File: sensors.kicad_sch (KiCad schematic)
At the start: 7 parts

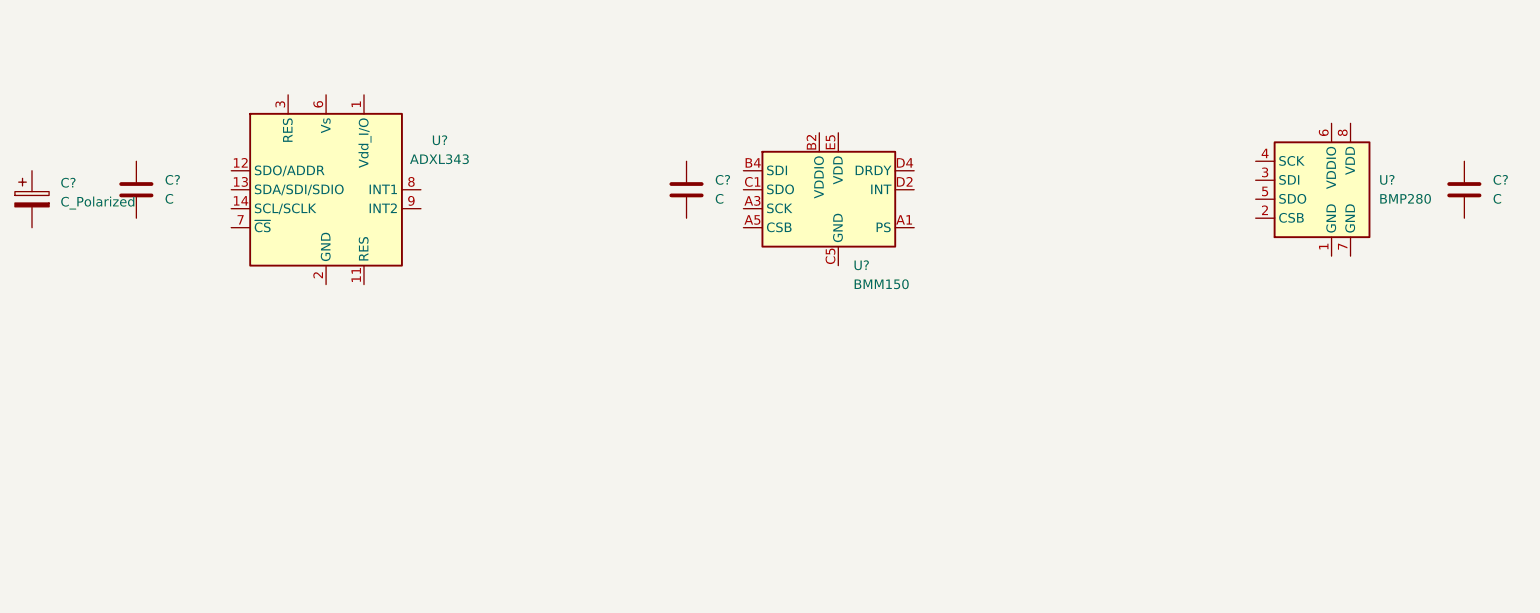
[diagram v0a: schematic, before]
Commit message: Refactor the mainboard
- Use smaller STM
- Use MPU-9250 as a motion sensor
- Connect some peripherals to the MCU
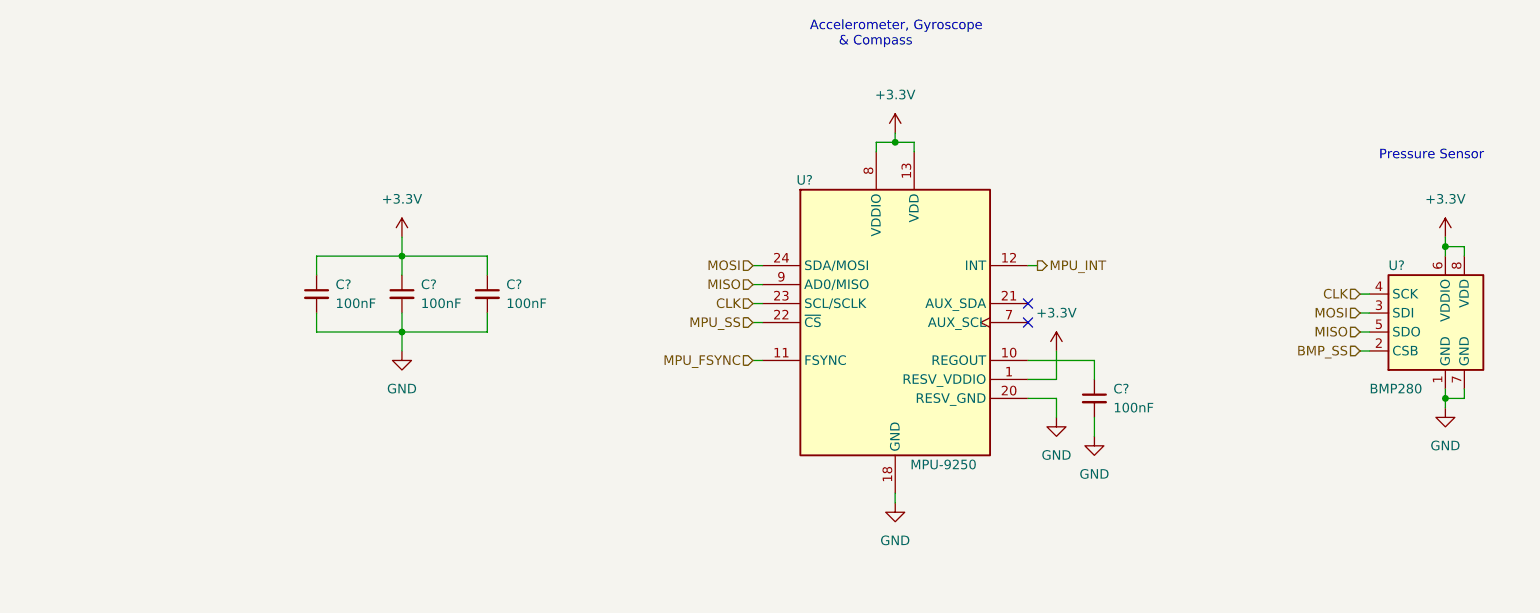
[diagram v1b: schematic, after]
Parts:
- removed C?: C_Polarized, symbol Device:C_Polarized
- removed C? (x3): C, symbol Device:C
- removed U?: BMM150, Package_CSP:WLCSP-12_1.56x1.56mm_P0.4mm, symbol Sensor_Magnetic:BMM150
- removed U?: ADXL343, Package_LGA:LGA-14_3x5mm_P0.8mm_LayoutBorder1x6y, symbol Sensor_Motion:ADXL343
- added C? (x4): 100nF, symbol Device:C_Small
- added U?: MPU-9250, Sensor_Motion:InvenSense_QFN-24_3x3mm_P0.4mm, symbol Sensor_Motion:MPU-9250
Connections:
- net GND: now reaches U?.1 (GND)
- net GND: now also U?.7 (GND), C?.2, C?.2, C?.2, C?.2, U?.18 (GND), U?.20 (RESV_GND)
- net BMP_SS: now reaches U?.2 (CSB)
- net MOSI: now reaches U?.3 (SDI)
- net MOSI: now also U?.24 (SDA/MOSI)
- net CLK: now reaches U?.4 (SCK)
- net CLK: now also U?.23 (SCL/SCLK)
- net MISO: now reaches U?.5 (SDO)
- net MISO: now also U?.9 (AD0/MISO)
- net +3.3V: now reaches U?.6 (VDDIO)
- net +3.3V: now also U?.8 (VDD), C?.1, C?.1, C?.1, U?.1 (RESV_VDDIO), U?.13 (VDD), U?.8 (VDDIO)
- new net: C?.1, U?.10 (REGOUT)
- new net MPU_FSYNC: U?.11 (FSYNC)
- new net MPU_INT: U?.12 (INT)
- new net MPU_SS: U?.22 (~{CS})
- no-connect marks 0 -> 2
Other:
- note added: "Accelerometer, Gyroscope & Compass"
- note added: "Pressure Sensor"
- moved on the sheet: U?

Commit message: Connect sensors to the MCU
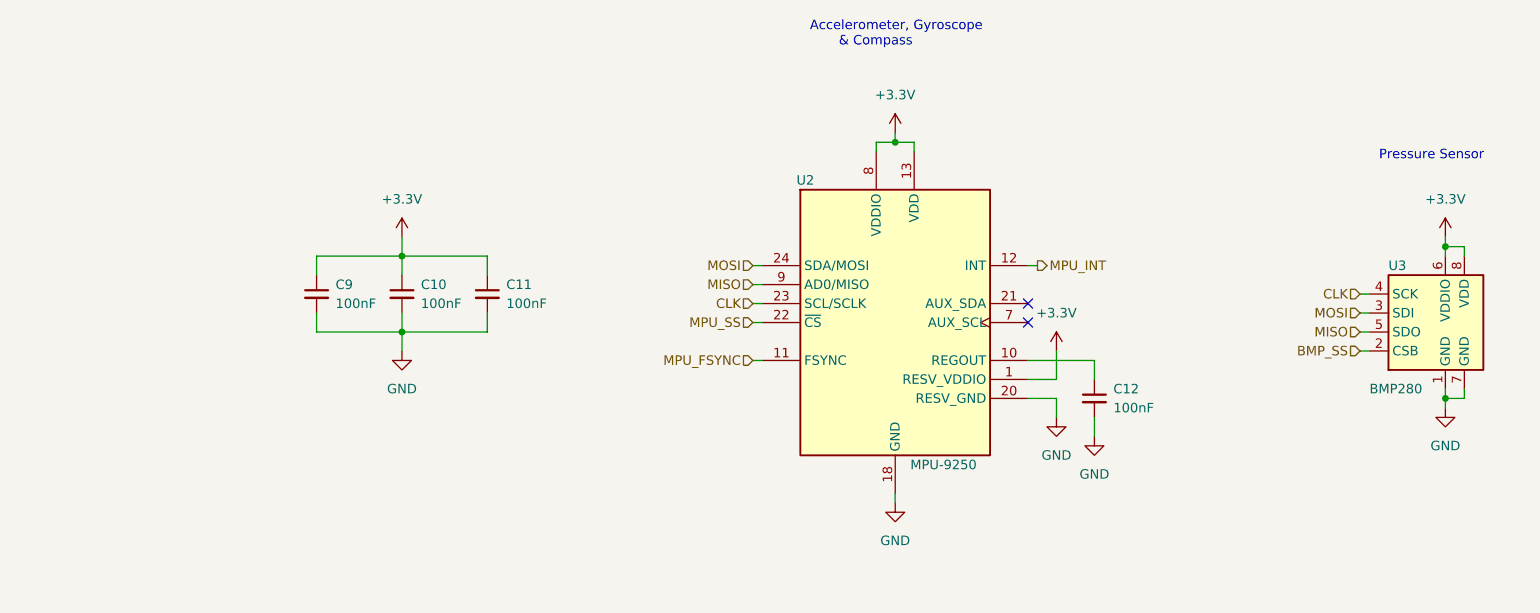
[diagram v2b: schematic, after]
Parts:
- gave numbers to parts that had none: 6
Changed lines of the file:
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@@
   (paper "A4")
   (title_block
-    (date "2022-11-22")
+    (date "2022-12-16")
     (rev "0.1.0")
   )
@@
   (symbol (lib_id "power:+3.3V") (at 222.25 81.28 0) (unit 1)
     (in_bom yes) (on_board yes) (fields_autoplaced)
-    (property "Reference" "#PWR?" (id 0) (at 222.25 85.09 0)
+    (property "Reference" "#PWR0120" (id 0) (at 222.25 85.09 0)
       (effects (font (size 1.27 1.27)) hide)
     )
@@
   (symbol (lib_id "Device:C_Small") (at 93.98 88.9 0) (unit 1)
     (in_bom yes) (on_board yes) (fields_autoplaced)
-    (property "Reference" "C?" (id 0) (at 96.52 87.6362 0)
+    (property "Reference" "C11" (id 0) (at 96.52 87.6362 0)
       (effects (font (size 1.27 1.27)) (justify left))
     )
@@
   (symbol (lib_id "power:+3.3V") (at 82.55 81.28 0) (unit 1)
     (in_bom yes) (on_board yes) (fields_autoplaced)
-    (property "Reference" "#PWR?" (id 0) (at 82.55 85.09 0)
+    (property "Reference" "#PWR0117" (id 0) (at 82.55 85.09 0)
       (effects (font (size 1.27 1.27)) hide)
     )
@@
   (symbol (lib_id "power:GND") (at 170.18 105.41 0) (unit 1)
     (in_bom yes) (on_board yes)
-    (property "Reference" "#PWR?" (id 0) (at 170.18 111.76 0)
+    (property "Reference" "#PWR0122" (id 0) (at 170.18 111.76 0)
       (effects (font (size 1.27 1.27)) hide)
     )
@@
   (symbol (lib_id "power:GND") (at 175.26 107.95 0) (unit 1)
     (in_bom yes) (on_board yes) (fields_autoplaced)
-    (property "Reference" "#PWR?" (id 0) (at 175.26 114.3 0)
+    (property "Reference" "#PWR0123" (id 0) (at 175.26 114.3 0)
       (effects (font (size 1.27 1.27)) hide)
     )
@@
   (symbol (lib_id "power:+3.3V") (at 170.18 96.52 0) (unit 1)
     (in_bom yes) (on_board yes) (fields_autoplaced)
-    (property "Reference" "#PWR?" (id 0) (at 170.18 100.33 0)
+    (property "Reference" "#PWR0121" (id 0) (at 170.18 100.33 0)
       (effects (font (size 1.27 1.27)) hide)
     )
@@
   (symbol (lib_id "power:GND") (at 148.59 116.84 0) (unit 1)
     (in_bom yes) (on_board yes) (fields_autoplaced)
-    (property "Reference" "#PWR?" (id 0) (at 148.59 123.19 0)
+    (property "Reference" "#PWR0116" (id 0) (at 148.59 123.19 0)
       (effects (font (size 1.27 1.27)) hide)
     )
@@
   (symbol (lib_id "Sensor_Pressure:BMP280") (at 222.25 93.98 0) (unit 1)
     (in_bom yes) (on_board yes)
-    (property "Reference" "U?" (id 0) (at 214.63 85.0899 0)
+    (property "Reference" "U3" (id 0) (at 214.63 85.0899 0)
       (effects (font (size 1.27 1.27)) (justify left))
     )
@@
   (symbol (lib_id "power:GND") (at 222.25 104.14 0) (unit 1)
     (in_bom yes) (on_board yes) (fields_autoplaced)
-    (property "Reference" "#PWR?" (id 0) (at 222.25 110.49 0)
+    (property "Reference" "#PWR0119" (id 0) (at 222.25 110.49 0)
       (effects (font (size 1.27 1.27)) hide)
     )
@@
   (symbol (lib_id "Device:C_Small") (at 175.26 102.87 0) (unit 1)
     (in_bom yes) (on_board yes) (fields_autoplaced)
-    (property "Reference" "C?" (id 0) (at 177.8 101.6062 0)
+    (property "Reference" "C12" (id 0) (at 177.8 101.6062 0)
       (effects (font (size 1.27 1.27)) (justify left))
     )
@@
   (symbol (lib_id "Device:C_Small") (at 82.55 88.9 0) (unit 1)
     (in_bom yes) (on_board yes) (fields_autoplaced)
-    (property "Reference" "C?" (id 0) (at 85.09 87.6362 0)
+    (property "Reference" "C10" (id 0) (at 85.09 87.6362 0)
       (effects (font (size 1.27 1.27)) (justify left))
     )
@@
   (symbol (lib_id "Device:C_Small") (at 71.12 88.9 0) (unit 1)
     (in_bom yes) (on_board yes) (fields_autoplaced)
-    (property "Reference" "C?" (id 0) (at 73.66 87.6362 0)
+    (property "Reference" "C9" (id 0) (at 73.66 87.6362 0)
       (effects (font (size 1.27 1.27)) (justify left))
     )
@@
   (symbol (lib_id "Sensor_Motion:MPU-9250") (at 148.59 92.71 0) (unit 1)
     (in_bom yes) (on_board yes)
-    (property "Reference" "U?" (id 0) (at 135.3694 73.66 0)
+    (property "Reference" "U2" (id 0) (at 135.3694 73.66 0)
       (effects (font (size 1.27 1.27)) (justify left))
     )
@@
   (symbol (lib_id "power:+3.3V") (at 148.59 67.31 0) (unit 1)
     (in_bom yes) (on_board yes) (fields_autoplaced)
-    (property "Reference" "#PWR?" (id 0) (at 148.59 71.12 0)
+    (property "Reference" "#PWR0118" (id 0) (at 148.59 71.12 0)
       (effects (font (size 1.27 1.27)) hide)
     )
@@
   (symbol (lib_id "power:GND") (at 82.55 96.52 0) (unit 1)
     (in_bom yes) (on_board yes) (fields_autoplaced)
-    (property "Reference" "#PWR?" (id 0) (at 82.55 102.87 0)
-      (effects (font (size 1.27 1.27)) hide)
-    )
+    (property "Reference" "#PWR0115" (id 0) (at 82.55 102.87 0)
+      (effects (font (size 1.27 1.27)) hide)
+    )

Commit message: Improve the power section:
- add ADC circuit to measure battery level
- add 5V LDO regulator
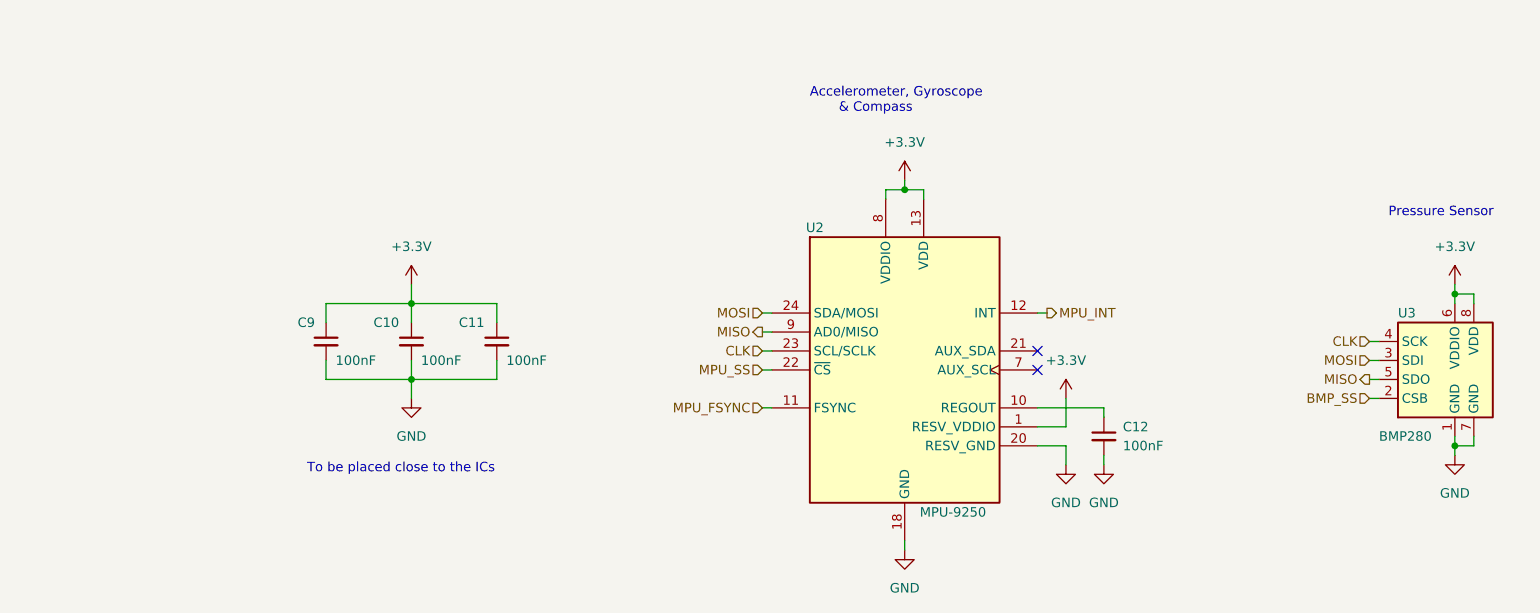
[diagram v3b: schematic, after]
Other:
- note added: "To be placed close to the ICs"
- title: (none) -> Sensors
- moved on the sheet: C10, C11, C12, C9, U2, U3

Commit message: Assign footprints to symbols
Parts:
- C17: renamed from C9; footprint (none) -> Capacitor_SMD:C_0603_1608Metric
- C18: renamed from C10; footprint (none) -> Capacitor_SMD:C_0603_1608Metric
- C19: renamed from C11; footprint (none) -> Capacitor_SMD:C_0603_1608Metric
- C20: renamed from C12; footprint (none) -> Capacitor_SMD:C_0603_1608Metric
- renumbered U2 to U7, U3 to U8
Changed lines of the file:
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@@
     (title "Sensors")
     (date "2022-12-17")
-    (rev "0.1.0")
+    (rev "${REVISION}")
   )
   (junction (at 223.52 88.9) (diameter 0) (color 0 0 0 0)
@@
   (symbol (lib_id "power:+3.3V") (at 223.52 87.63 0) (unit 1)
     (in_bom yes) (on_board yes) (fields_autoplaced)
-    (property "Reference" "#PWR017" (id 0) (at 223.52 91.44 0)
+    (property "Reference" "#PWR044" (id 0) (at 223.52 91.44 0)
       (effects (font (size 1.27 1.27)) hide)
     )
@@
   (symbol (lib_id "Device:C_Small") (at 95.25 95.25 0) (unit 1)
     (in_bom yes) (on_board yes)
-    (property "Reference" "C11" (id 0) (at 90.17 92.7162 0)
+    (property "Reference" "C19" (id 0) (at 90.17 92.7162 0)
       (effects (font (size 1.27 1.27)) (justify left))
     )
@@
       (effects (font (size 1.27 1.27)) (justify left))
     )
-    (property "Footprint" "" (id 2) (at 95.25 95.25 0)
+    (property "Footprint" "Capacitor_SMD:C_0603_1608Metric" (id 2) (at 95.25 95.25 0)
       (effects (font (size 1.27 1.27)) hide)
     )
@@
   (symbol (lib_id "power:+3.3V") (at 83.82 87.63 0) (unit 1)
     (in_bom yes) (on_board yes) (fields_autoplaced)
-    (property "Reference" "#PWR016" (id 0) (at 83.82 91.44 0)
+    (property "Reference" "#PWR043" (id 0) (at 83.82 91.44 0)
       (effects (font (size 1.27 1.27)) hide)
     )
@@
   (symbol (lib_id "power:GND") (at 171.45 111.76 0) (unit 1)
     (in_bom yes) (on_board yes)
-    (property "Reference" "#PWR021" (id 0) (at 171.45 118.11 0)
+    (property "Reference" "#PWR048" (id 0) (at 171.45 118.11 0)
       (effects (font (size 1.27 1.27)) hide)
     )
@@
   (symbol (lib_id "power:GND") (at 176.53 111.76 0) (unit 1)
     (in_bom yes) (on_board yes) (fields_autoplaced)
-    (property "Reference" "#PWR022" (id 0) (at 176.53 118.11 0)
+    (property "Reference" "#PWR049" (id 0) (at 176.53 118.11 0)
       (effects (font (size 1.27 1.27)) hide)
     )
@@
   (symbol (lib_id "power:+3.3V") (at 171.45 102.87 0) (unit 1)
     (in_bom yes) (on_board yes) (fields_autoplaced)
-    (property "Reference" "#PWR019" (id 0) (at 171.45 106.68 0)
+    (property "Reference" "#PWR046" (id 0) (at 171.45 106.68 0)
       (effects (font (size 1.27 1.27)) hide)
     )
@@
   (symbol (lib_id "power:GND") (at 149.86 123.19 0) (unit 1)
     (in_bom yes) (on_board yes) (fields_autoplaced)
-    (property "Reference" "#PWR023" (id 0) (at 149.86 129.54 0)
+    (property "Reference" "#PWR050" (id 0) (at 149.86 129.54 0)
       (effects (font (size 1.27 1.27)) hide)
     )
@@
   (symbol (lib_id "Sensor_Pressure:BMP280") (at 223.52 100.33 0) (unit 1)
     (in_bom yes) (on_board yes)
-    (property "Reference" "U3" (id 0) (at 215.9 91.4399 0)
+    (property "Reference" "U8" (id 0) (at 215.9 91.4399 0)
       (effects (font (size 1.27 1.27)) (justify left))
     )
@@
   (symbol (lib_id "power:GND") (at 223.52 110.49 0) (unit 1)
     (in_bom yes) (on_board yes) (fields_autoplaced)
-    (property "Reference" "#PWR020" (id 0) (at 223.52 116.84 0)
+    (property "Reference" "#PWR047" (id 0) (at 223.52 116.84 0)
       (effects (font (size 1.27 1.27)) hide)
     )
@@
   (symbol (lib_id "Device:C_Small") (at 176.53 107.95 0) (unit 1)
     (in_bom yes) (on_board yes) (fields_autoplaced)
-    (property "Reference" "C12" (id 0) (at 179.07 106.6862 0)
+    (property "Reference" "C20" (id 0) (at 179.07 106.6862 0)
       (effects (font (size 1.27 1.27)) (justify left))
     )
@@
       (effects (font (size 1.27 1.27)) (justify left))
     )
-    (property "Footprint" "" (id 2) (at 176.53 107.95 0)
+    (property "Footprint" "Capacitor_SMD:C_0603_1608Metric" (id 2) (at 176.53 107.95 0)
       (effects (font (size 1.27 1.27)) hide)
     )
@@
   (symbol (lib_id "Device:C_Small") (at 83.82 95.25 0) (unit 1)
     (in_bom yes) (on_board yes)
-    (property "Reference" "C10" (id 0) (at 78.74 92.7162 0)
+    (property "Reference" "C18" (id 0) (at 78.74 92.7162 0)
       (effects (font (size 1.27 1.27)) (justify left))
     )
@@
       (effects (font (size 1.27 1.27)) (justify left))
     )
-    (property "Footprint" "" (id 2) (at 83.82 95.25 0)
+    (property "Footprint" "Capacitor_SMD:C_0603_1608Metric" (id 2) (at 83.82 95.25 0)
       (effects (font (size 1.27 1.27)) hide)
     )
@@
   (symbol (lib_id "Device:C_Small") (at 72.39 95.25 0) (unit 1)
     (in_bom yes) (on_board yes)
-    (property "Reference" "C9" (id 0) (at 68.58 92.7162 0)
+    (property "Reference" "C17" (id 0) (at 68.58 92.7162 0)
       (effects (font (size 1.27 1.27)) (justify left))
     )
@@
       (effects (font (size 1.27 1.27)) (justify left))
     )
-    (property "Footprint" "" (id 2) (at 72.39 95.25 0)
+    (property "Footprint" "Capacitor_SMD:C_0603_1608Metric" (id 2) (at 72.39 95.25 0)
       (effects (font (size 1.27 1.27)) hide)
     )
@@
   (symbol (lib_id "Sensor_Motion:MPU-9250") (at 149.86 99.06 0) (unit 1)
     (in_bom yes) (on_board yes)
-    (property "Reference" "U2" (id 0) (at 136.6394 80.01 0)
+    (property "Reference" "U7" (id 0) (at 136.6394 80.01 0)
       (effects (font (size 1.27 1.27)) (justify left))
     )
@@
   (symbol (lib_id "power:+3.3V") (at 149.86 73.66 0) (unit 1)
     (in_bom yes) (on_board yes) (fields_autoplaced)
-    (property "Reference" "#PWR015" (id 0) (at 149.86 77.47 0)
+    (property "Reference" "#PWR042" (id 0) (at 149.86 77.47 0)
       (effects (font (size 1.27 1.27)) hide)
     )
@@
   (symbol (lib_id "power:GND") (at 83.82 102.87 0) (unit 1)
     (in_bom yes) (on_board yes) (fields_autoplaced)
-    (property "Reference" "#PWR018" (id 0) (at 83.82 109.22 0)
-      (effects (font (size 1.27 1.27)) hide)
-    )
+    (property "Reference" "#PWR045" (id 0) (at 83.82 109.22 0)
+      (effects (font (size 1.27 1.27)) hide)
+    )
